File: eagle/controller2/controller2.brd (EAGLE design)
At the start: 88.9 x 52.1 mm, 21 parts, among them U1 ATMEGA328P_PDIP

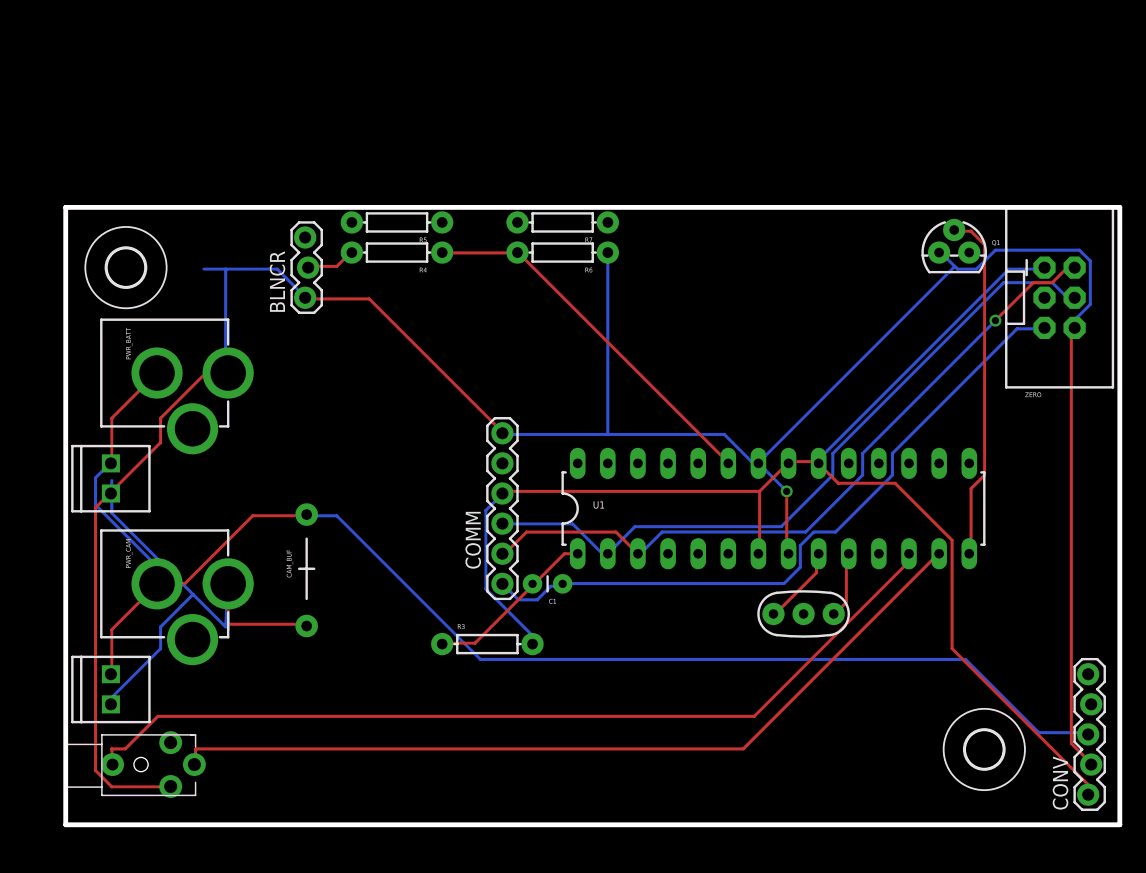
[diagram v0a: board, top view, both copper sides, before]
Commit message: eagle: new board layout
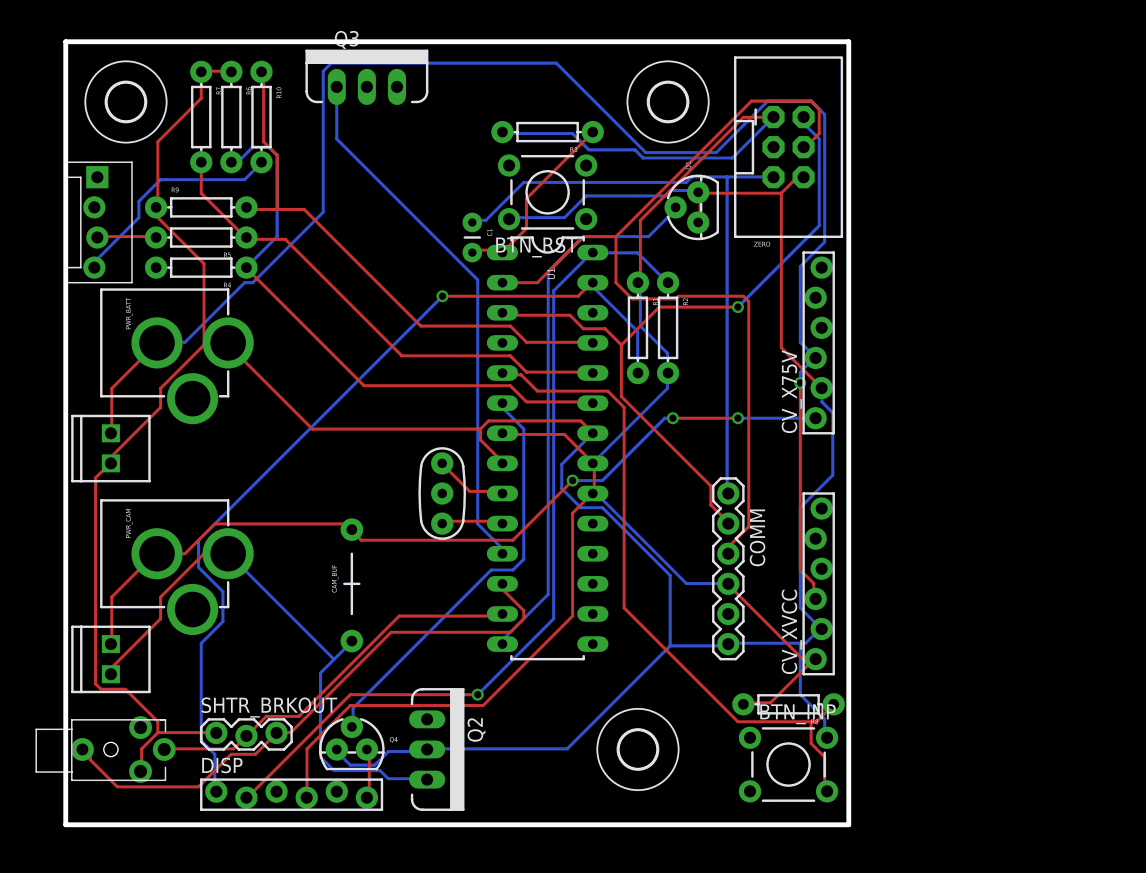
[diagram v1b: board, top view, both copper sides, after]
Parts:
- removed BLNCR: (no value), SparkFun-Connectors:1X03_LOCK
- removed CONV: (no value), SparkFun-Connectors:1X05_LOCK
- added BTN_INP, BTN_RST: (no value), SparkFun-Retired:TACTILE-PTH
- added CV_X75V, CV_XVCC, DISP: (no value), SparkFun-Connectors:1X06_FEMALE_LOCK.010
- added H3: MOUNT-HOLE3.2, holes:3,2
- added J1: (no value), SparkFun-Connectors:MOLEX-1X4_LOCK
- added Q2, Q3: MOSFET-NCHANNELFQP30N06L, SparkFun-DiscreteSemi:TO220V
- added Q4: (no value), SparkFun-DiscreteSemi:TO-92
- added R1, R10, R2, R8, R9: (no value), SparkFun-Resistors:AXIAL-0.3
- added SHTR_BRKOUT: (no value), SparkFun-Connectors:1X03_LOCK
- moved R3 43.5 mm to (40.6, 58.4), turned to 180 degrees
- moved Y1 32.1 mm to (31.8, 27.9), turned to 270 degrees
- moved R7 31.8 mm to (11.4, 59.7), turned to 270 degrees
- moved C1 31.4 mm to (34.3, 50.8), turned to 270 degrees
- moved R6 30.2 mm to (14.0, 59.7), turned to 270 degrees
- moved H1 29.2 mm to (48.3, 6.35)
- moved ZERO 26.2 mm to (61.0, 57.1)
- moved Q1 21.9 mm to (53.3, 52.1), turned to 90 degrees
- moved COMM 20.5 mm to (55.9, 27.9), turned to 270 degrees
- moved U1 19.7 mm to (40.6, 31.8), turned to 270 degrees
- moved R4 16.6 mm to (11.4, 47.0)
- moved R5 16.6 mm to (11.4, 49.5)
- moved H2 14.0 mm to (5.08, 61.0)
- moved CAM_BUF 4.02 mm to (24.1, 20.3)
- moved CAM_SHTR 2.84 mm to (3.81, 6.35)
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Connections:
- removed net N$7: CAM_BUF.2, CONV.3, PWR_BATT.GND, PWR_CAM.GND, ST_BATT.P1, ST_CAM.P1
- new net BATT_VCC: CV_X75V.3, CV_XVCC.3, PWR_BATT.GND, ST_BATT.P1
- new net BTN_INP: BTN_INP.4, R8.P$1, U1.5
- new net CAM_EN: Q2.1
- new net CAM_VCC: CAM_BUF.2, CV_X75V.1, PWR_CAM.GND, ST_CAM.P1
- new net CELL3: R10.P$1, R9.P$2, U1.25
- new net DISP_EN: Q4.2, U1.6
- new net DISP_RST: DISP.3
- new net EXT: Q3.3
- new net EXT_EN: Q3.1, U1.11
- new net N$10: DISP.5
- new net N$2: BTN_RST.4
- new net N$3: DISP.6, Q4.3
- new net N$5: J1.4, R10.P$2
- new net SCL: DISP.2, R2.P$1, U1.28
- new net SDA: DISP.1, R1.P$2, U1.27
- net CAM1: now also SHTR_BRKOUT.2
- net CAM2: now also SHTR_BRKOUT.3
- net CAM_OUT: now also Q2.3
- net GND: now also BTN_INP.2, BTN_RST.2, CV_X75V.2, CV_XVCC.2, Q1.3, Q2.2, Q4.1, R9.P$1, SHTR_BRKOUT.1; no longer BLNCR.1, CONV.2
- net N$11: no longer BLNCR.2
- net N$12: now also J1.3; no longer BLNCR.3
- net VCC: now also CV_XVCC.1, DISP.4, R1.P$1, R2.P$2, R8.P$2; no longer CONV.1
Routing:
- net BATT_VCC: track 0.00 -> 131.0 mm, vias 0 -> 1
- net N$7: track 120.1 -> 0.00 mm
- net SDA: track 0.00 -> 74.8 mm, vias 0 -> 1
- net SCL: track 0.00 -> 71.8 mm, vias 0 -> 1
- net CAM_VCC: track 0.00 -> 70.8 mm, vias 0 -> 3
- net BTN_INP: track 0.00 -> 57.1 mm
- net GND: track 214.6 -> 268.7 mm, vias 1 -> 0
- net CELL3: track 0.00 -> 46.1 mm
- net EXT_EN: track 0.00 -> 45.2 mm
- net CELL2: track 0.00 -> 41.9 mm
- net CAM1: track 70.8 -> 33.3 mm
- net VCC: track 114.5 -> 150.9 mm
- net DISP_EN: track 0.00 -> 35.1 mm
- net CAM2: track 75.8 -> 48.2 mm
- net N$5: track 0.00 -> 18.9 mm
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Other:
- board size 88.9 x 52.1 mm -> 66 x 66 mm

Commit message: controller2: EXT circuit
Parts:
- added 3.3V, 5V: (no value), SparkFun-Connectors:1X02_LOCK
- added ST_BATT1: (no value), SparkFun-Connectors:1X02_2.54_SCREWTERM
- moved Q3 7.62 mm to (33.0, 62.2)
- moved Y1 4.02 mm to (30.5, 31.8), turned to 180 degrees
- moved SHTR_BRKOUT 1.27 mm to (11.4, 7.62), turned to 90 degrees
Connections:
- removed net N$10: DISP.5
- new net BTN1: U1.11
- new net BTN2: U1.12
- new net BTN3: U1.13
- new net N$6: 5V.1, DISP.5
- new net N$7: 3.3V.2, DISP.4
- net BATT_VCC: now also ST_BATT1.P1
- net BTN_INP: no longer U1.5
- net CAM1: now also U1.14; no longer U1.13
- net CAM2: now also U1.15; no longer U1.12
- net CAM_EN: now also U1.5
- net EXT: now also ST_BATT1.P2
- net EXT_EN: now also U1.4; no longer U1.11
- net GND: now also J1.1
- net N$11: now also J1.2
- net VCC: now also 3.3V.1, 5V.2; no longer DISP.4
- net ZERO_EN: now also U1.26; no longer U1.14
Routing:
- net BTN_INP: track 57.1 -> 8.70 mm
- net ZERO_EN: track 46.2 -> 11.8 mm
- net CAM_EN: track 0.00 -> 31.9 mm
- net SCL: track 71.8 -> 97.6 mm
- net BATT_VCC: track 131.0 -> 107.5 mm, vias 1 -> 0
- net EXT_EN: track 45.2 -> 24.3 mm
- net EXT: track 0.00 -> 15.7 mm
- net CELL3: track 46.1 -> 60.4 mm
- net CAM_OUT: track 48.7 -> 59.4 mm
- net RST: track 53.8 -> 62.6 mm
- net TX: track 60.6 -> 68.9 mm, vias 1 -> 0
- net VCC: track 150.9 -> 159.1 mm
- net N$7: track 0.00 -> 7.51 mm
- net N$11: track 0.00 -> 7.35 mm
- net N$6: track 0.00 -> 6.23 mm
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
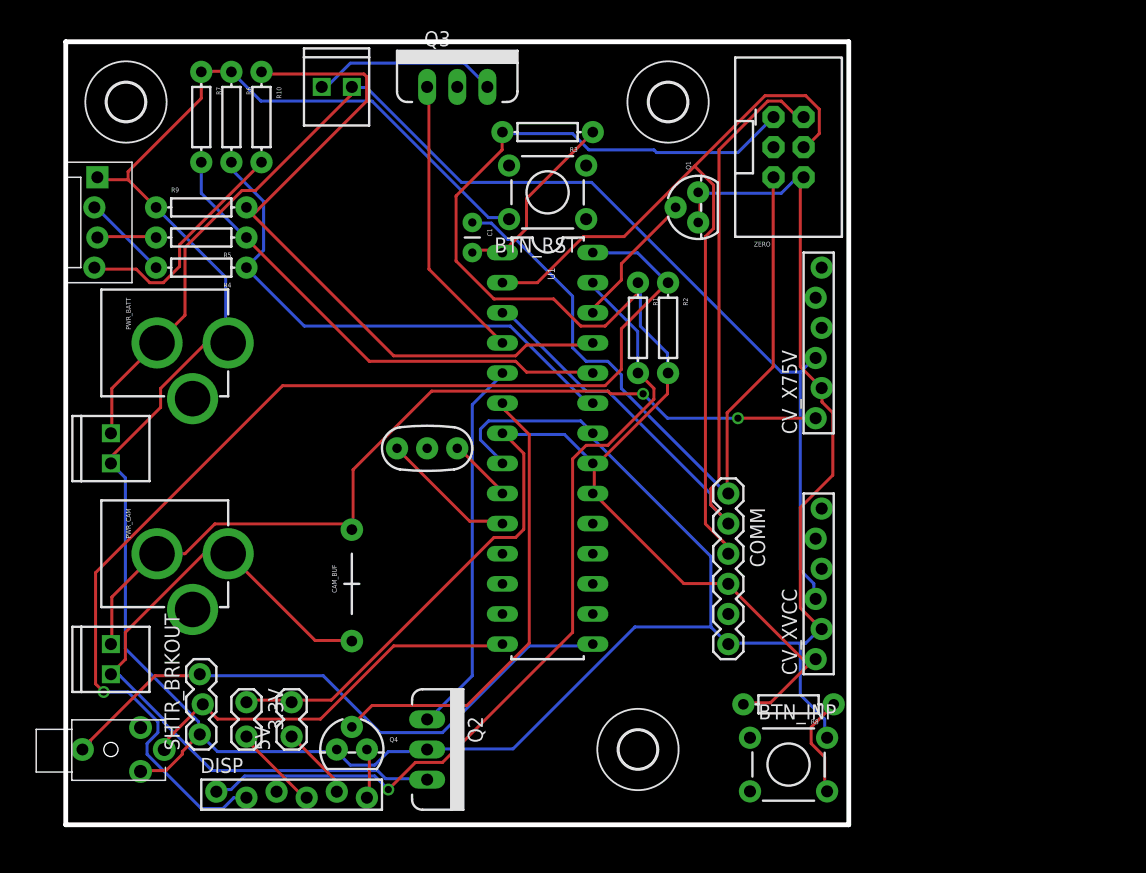
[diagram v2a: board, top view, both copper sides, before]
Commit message: controller2: 3.5mm headphone jack
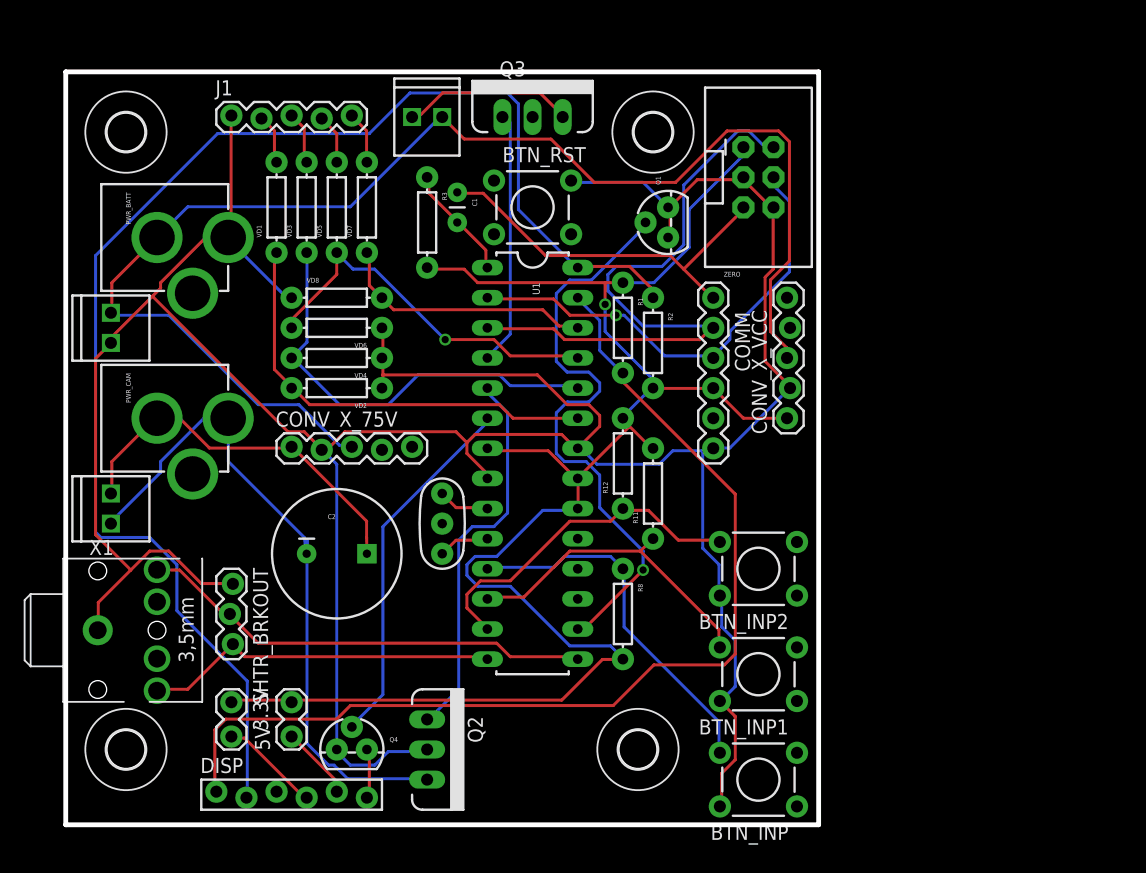
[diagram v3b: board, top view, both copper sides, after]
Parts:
- removed CAM_BUF: 4700uF, SparkFun-Capacitors:CAP-PTH-LARGE
- removed CAM_SHTR: (no value), SparkFun-Connectors:STEREOJACK2.5MM_STEREOJACK2.5MM
- removed CV_X75V, CV_XVCC: (no value), SparkFun-Connectors:1X06_FEMALE_LOCK.010
- removed R10, R4, R5, R6, R7, R9: (no value), SparkFun-Resistors:AXIAL-0.3
- added BTN_INP1, BTN_INP2: (no value), SparkFun-Retired:TACTILE-PTH
- added C2: (no value), SparkFun-Passives:CPOL-RADIAL-1000UF-25V
- added CONV_X_75V, CONV_X_VCC: (no value), SparkFun-Connectors:1X05_LOCK
- added H4: MOUNT-HOLE3.2, holes:3,2
- added R11, R12, VD1, VD2, VD3, VD4, VD5, VD6, VD7, VD8: (no value), SparkFun-Resistors:AXIAL-0.3
- added X1: STEREOJACK, adafruit:STX3100
- COMM: value FTDI_BASICPTH -> (none)
- J1: device SparkFun-Connectors:MOLEX-1X4_LOCK -> SparkFun-Connectors:1X05_LOCK
- PWR_BATT, PWR_CAM: value POWER_JACKPTH -> (none)
- Q2, Q3: value MOSFET-NCHANNELFQP30N06L -> (none)
- moved COMM 16.6 mm to (54.6, 44.5)
- moved R8 15.9 mm to (47.0, 17.8), turned to 270 degrees
- moved SHTR_BRKOUT 13.0 mm to (14.0, 20.3), turned to 270 degrees
- moved R3 12.7 mm to (30.5, 50.8), turned to 270 degrees
- moved ST_CAM 12.7 mm to (3.81, 25.4)
- moved J1 12.5 mm to (14.0, 59.7), turned to 0 degrees
- moved PWR_CAM 11.4 mm to (0.00, 34.3)
- moved ST_BATT 10.2 mm to (3.81, 40.6)
- moved PWR_BATT 8.89 mm to (0.00, 49.5)
- moved ST_BATT1 8.03 mm to (29.2, 59.7)
- moved Q3 6.84 mm to (39.4, 59.7)
- moved Y1 6.48 mm to (31.8, 25.4), turned to 270 degrees
- moved ZERO 3.59 mm to (58.4, 54.6)
- moved Q1 2.84 mm to (50.8, 50.8)
- moved C1 2.84 mm to (33.0, 53.3)
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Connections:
- removed net BTN_INP: BTN_INP.4, R8.P$1
- removed net N$12: J1.3, R5.P$2
- new net CELL4: U1.26, VD7.P$1, VD8.P$2
- new net N$10: J1.4, VD5.P$2
- net BATT_VCC: now also CONV_X_75V.3, CONV_X_VCC.3; no longer CV_X75V.3, CV_XVCC.3
- net BTN1: now also BTN_INP.4, R8.P$1
- net BTN2: now also BTN_INP1.4, R11.P$1
- net BTN3: now also BTN_INP2.4, R12.P$1
- net CAM1: now also SHTR_BRKOUT.3, X1.5; no longer CAM_SHTR.TIP, SHTR_BRKOUT.2
- net CAM2: now also SHTR_BRKOUT.2, X1.2; no longer CAM_SHTR.SHIELD, SHTR_BRKOUT.3
- net CAM_OUT: now also C2.2; no longer CAM_BUF.1
- net CAM_VCC: now also C2.1, CONV_X_75V.1; no longer CAM_BUF.2, CV_X75V.1
- net CELL1: now also VD1.P$1, VD2.P$2; no longer R4.P$1, R6.P$2
- net CELL2: now also VD3.P$1, VD4.P$2; no longer R5.P$1, R7.P$2
- net CELL3: now also VD5.P$1, VD6.P$2; no longer R10.P$1, R9.P$2
- net GND: now also BTN_INP1.2, BTN_INP2.2, CONV_X_75V.2, CONV_X_VCC.2, VD2.P$1, VD4.P$1, VD6.P$1, VD8.P$1, X1.1, ZERO.3; no longer CAM_SHTR.RING1, CV_X75V.2, CV_XVCC.2, R6.P$1, R7.P$1, R9.P$1
- net N$11: now also J1.5, VD7.P$2; no longer J1.2, R4.P$2
- net N$4: now also J1.2, VD1.P$2; no longer ZERO.3
- net N$5: now also J1.3, VD3.P$2; no longer J1.4, R10.P$2
- net VCC: now also CONV_X_VCC.1, R11.P$2, R12.P$2; no longer CV_XVCC.1
- net ZERO_EN: now also U1.16; no longer U1.26
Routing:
- net CAM_VCC: track 75.2 -> 32.1 mm, vias 2 -> 0
- net ZERO_EN: track 11.8 -> 50.5 mm, vias 0 -> 1
- net RX: track 72.1 -> 39.6 mm, vias 0 -> 1
- net BTN1: track 0.00 -> 31.2 mm
- net RST: track 62.6 -> 32.5 mm
- net BTN3: track 0.00 -> 29.2 mm
- net CELL3: track 60.4 -> 31.9 mm, vias 0 -> 1
- net BTN2: track 0.00 -> 27.0 mm
- net CELL4: track 0.00 -> 22.0 mm
- net SCL: track 97.6 -> 119.1 mm, vias 1 -> 0
- net N$5: track 19.9 -> 4.49 mm
- net SDA: track 72.2 -> 87.3 mm, vias 1 -> 0
- net TX: track 68.9 -> 53.9 mm
- net VCC: track 159.1 -> 146.1 mm, vias 0 -> 1
- net CAM2: track 51.0 -> 38.6 mm
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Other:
- board size 66 x 66 mm -> 63.5 x 63.5 mm

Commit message: controller2: eagle layout nicely routed
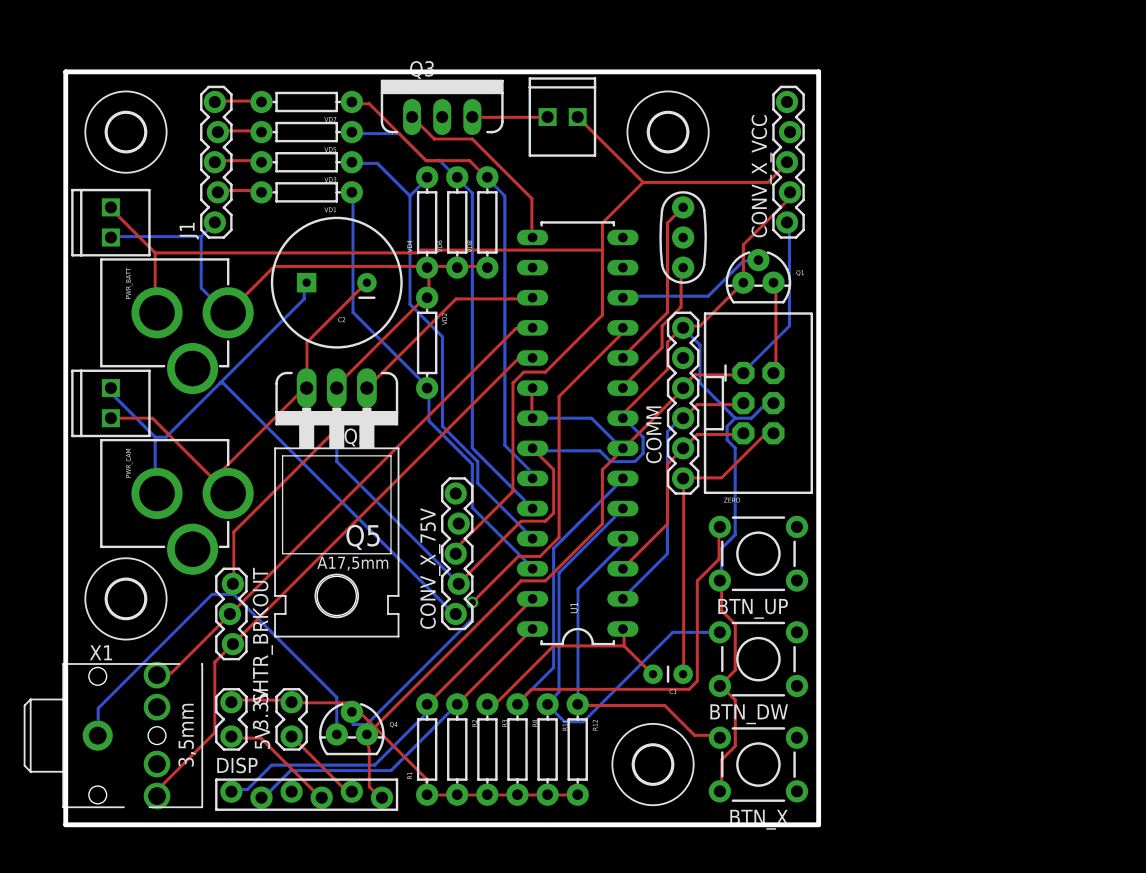
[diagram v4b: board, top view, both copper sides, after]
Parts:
- removed BTN_INP, BTN_INP1, BTN_INP2, BTN_RST: (no value), SparkFun-Retired:TACTILE-PTH
- added BTN_DW, BTN_UP, BTN_X: (no value), SparkFun-Retired:TACTILE-PTH
- added Q5: (no value), transistor-power:TO220BH
- moved H2 69.4 mm to (49.5, 5.08)
- moved H1 67.6 mm to (5.08, 58.4)
- moved C1 44.9 mm to (52.1, 12.7), turned to 180 degrees
- moved R3 44.7 mm to (35.6, 6.35)
- moved R1 39.2 mm to (30.5, 6.35), turned to 90 degrees
- moved R2 38.1 mm to (33.0, 6.35)
- moved Y1 31.5 mm to (52.1, 49.5), turned to 90 degrees
- moved Q2 31.4 mm to (22.9, 36.8), turned to 180 degrees
- moved R12 24.4 mm to (43.2, 6.35), turned to 270 degrees
- moved R11 23.3 mm to (40.6, 6.35), turned to 270 degrees
- moved C2 22.9 mm to (22.9, 45.7), turned to 180 degrees
- moved CONV_X_75V 19.8 mm to (33.0, 17.8), turned to 90 degrees
- moved ZERO 19.0 mm to (58.4, 35.6)
- moved CONV_X_VCC 16.5 mm to (61.0, 50.8)
- moved COMM 15.5 mm to (52.1, 29.2), turned to 90 degrees
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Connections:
- removed net N$2: BTN_RST.4
- new net FOO4: U1.13
- new net FOO5: U1.16
- new net FOO9: U1.14
- new net N$12: Q1.3, ZERO.2
- net BTN1: now also BTN_UP.4, U1.6; no longer BTN_INP.4, U1.11
- net BTN2: now also BTN_DW.4, U1.5; no longer BTN_INP1.4, U1.12
- net BTN3: now also BTN_X.4, U1.4; no longer BTN_INP2.4, U1.13
- net CAM1: now also U1.19; no longer U1.14
- net CAM2: now also U1.18; no longer U1.15
- net CAM_EN: now also U1.17; no longer U1.5
- net CELL1: now also U1.26; no longer U1.23
- net CELL2: now also U1.25; no longer U1.24
- net CELL3: now also U1.24; no longer U1.25
- net CELL4: now also U1.23; no longer U1.26
- net DISP_EN: now also U1.11; no longer U1.6
- net EXT_EN: now also U1.15; no longer U1.4
- net GND: now also BTN_DW.2, BTN_UP.2, BTN_X.2, ZERO.4; no longer BTN_INP.2, BTN_INP1.2, BTN_INP2.2, BTN_RST.2, Q1.3, ZERO.3, ZERO.6
- net RST: now also ZERO.6; no longer ZERO.5
- net RX: now also ZERO.3; no longer ZERO.4
- net TX: now also ZERO.5; no longer ZERO.2
- net ZERO_EN: now also U1.12; no longer U1.16
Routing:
- net SCL: track 119.1 -> 28.8 mm
- net SDA: track 87.3 -> 32.5 mm
- net VCC: track 146.1 -> 105.5 mm, vias 1 -> 0
- net GND: track 273.7 -> 234.4 mm
- net ZERO_EN: track 50.5 -> 12.7 mm, vias 1 -> 0
- net TX: track 53.9 -> 17.9 mm
- net CAM_VCC: track 32.1 -> 57.4 mm
- net CAM_OUT: track 58.0 -> 36.5 mm
- net BTN1: track 31.2 -> 52.5 mm
- net CAM1: track 30.1 -> 50.7 mm
- net CELL4: track 22.0 -> 41.0 mm
- net RX: track 39.6 -> 23.1 mm, vias 1 -> 0
- net CAM_EN: track 32.6 -> 17.1 mm
- net DISP_EN: track 30.8 -> 45.7 mm, vias 0 -> 1
- net N$8: track 4.34 -> 14.8 mm
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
